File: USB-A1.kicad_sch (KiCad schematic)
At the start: 24 parts, among them J10 USB3_A, J9 USB3_A, U16 UCS2114-1-V/G4, U17 TPD4E02B04DQA, U18 TPD4E02B04DQA

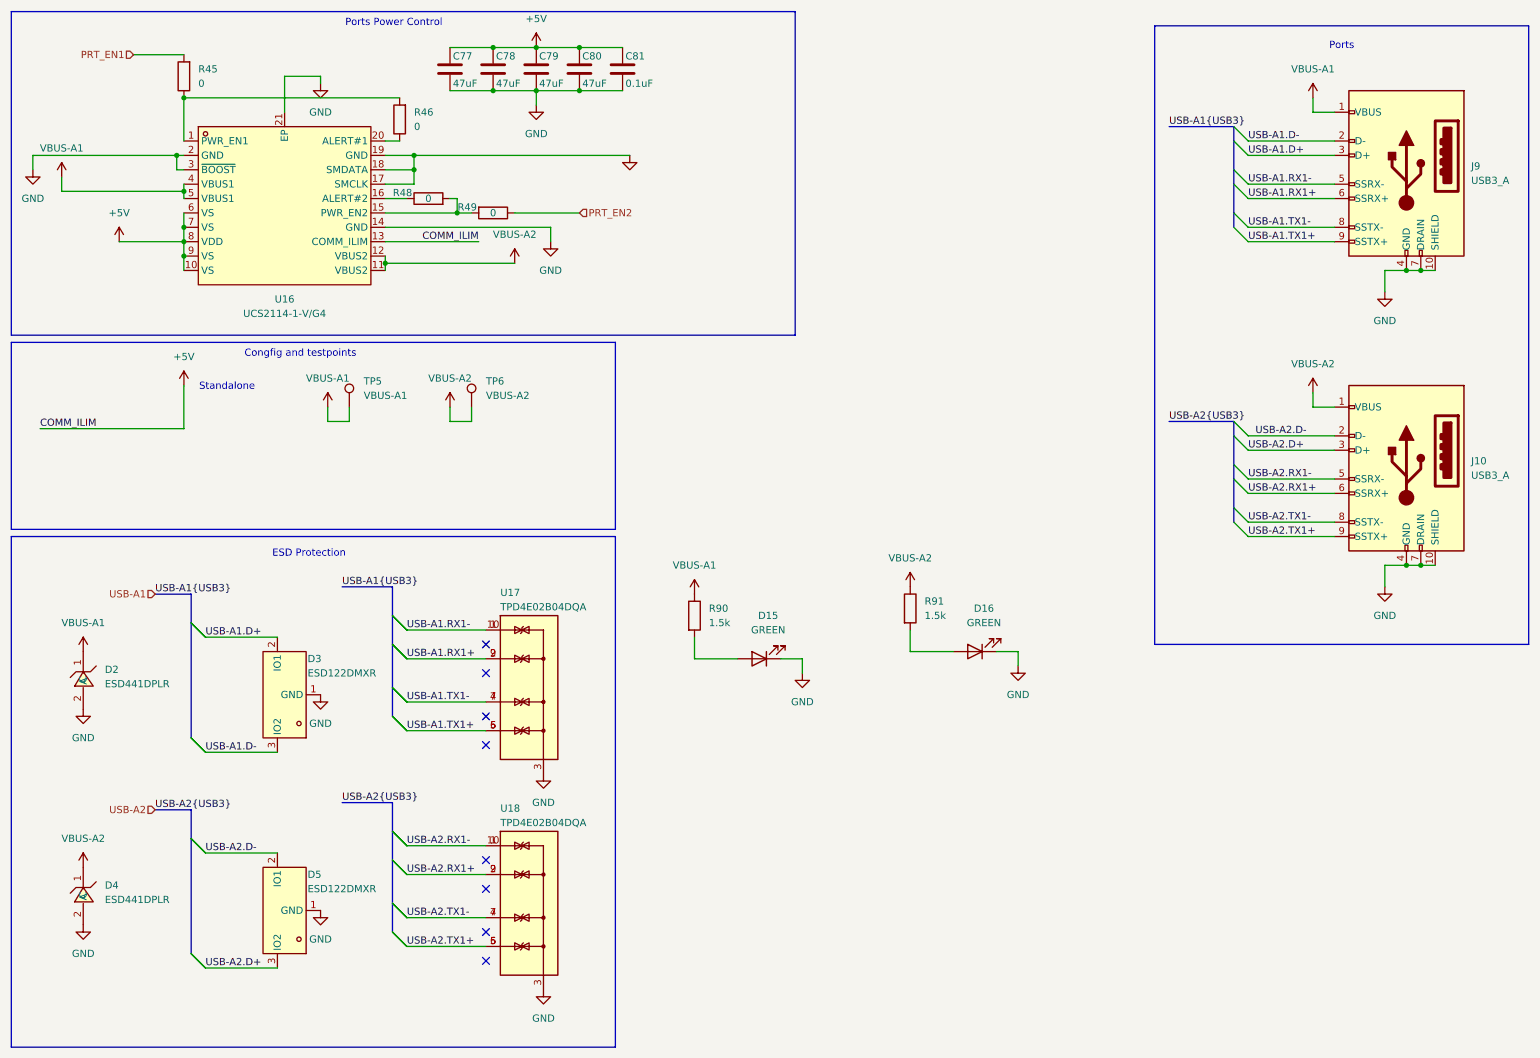
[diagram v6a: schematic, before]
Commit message: Ferrite Breads added for 5V, TVS and ESD diodes added
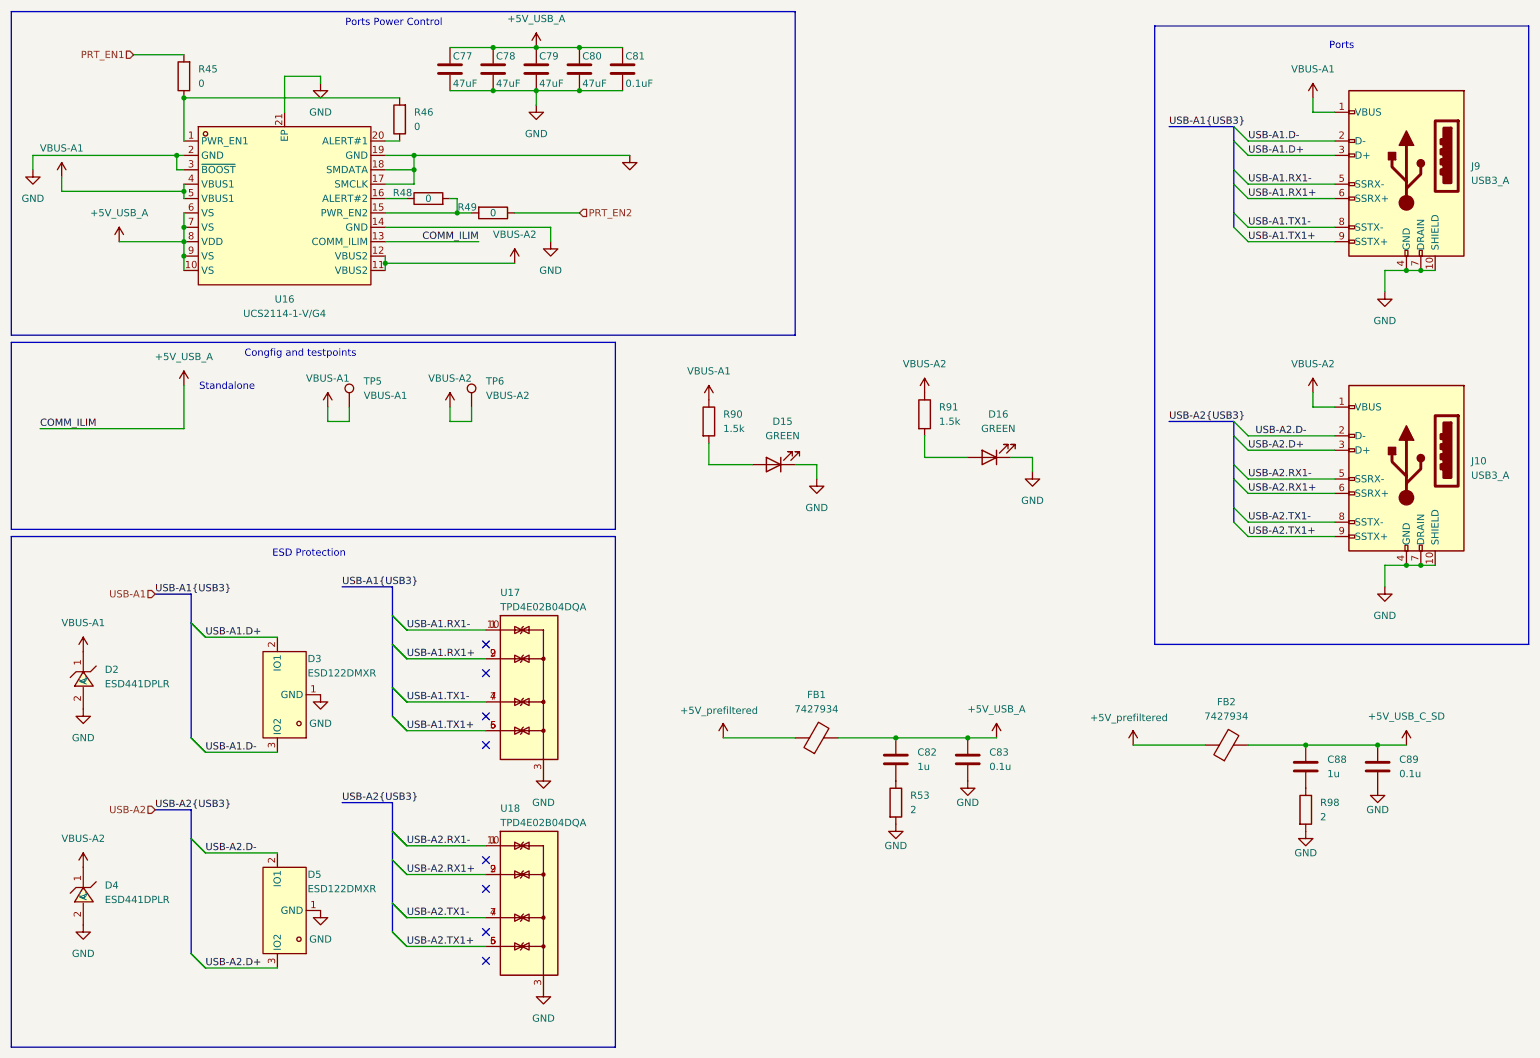
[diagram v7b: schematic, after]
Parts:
- added C82, C88: 1u, symbol Device:C
- added C83, C89: 0.1u, symbol Device:C
- added FB1, FB2: 7427934, symbol Device:FerriteBead
- added R53, R98: 2, symbol Device:R
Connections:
- net GND: now also C83.2, C89.2, R53.2, R98.2
- net +5V renamed +5V_USB_A
- net +5V_USB_A: now also C82.1, C83.1, FB1.2
- new net: C82.2, R53.1
- new net: C88.2, R98.1
- new net +5V_USB_C_SD: C88.1, C89.1, FB2.2
- new net +5V_prefiltered: FB1.1, FB2.1
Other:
- moved on the sheet: D15, D16, R90, R91

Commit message: Ferrite bread filter for LDO and MIC23201, labelling improved
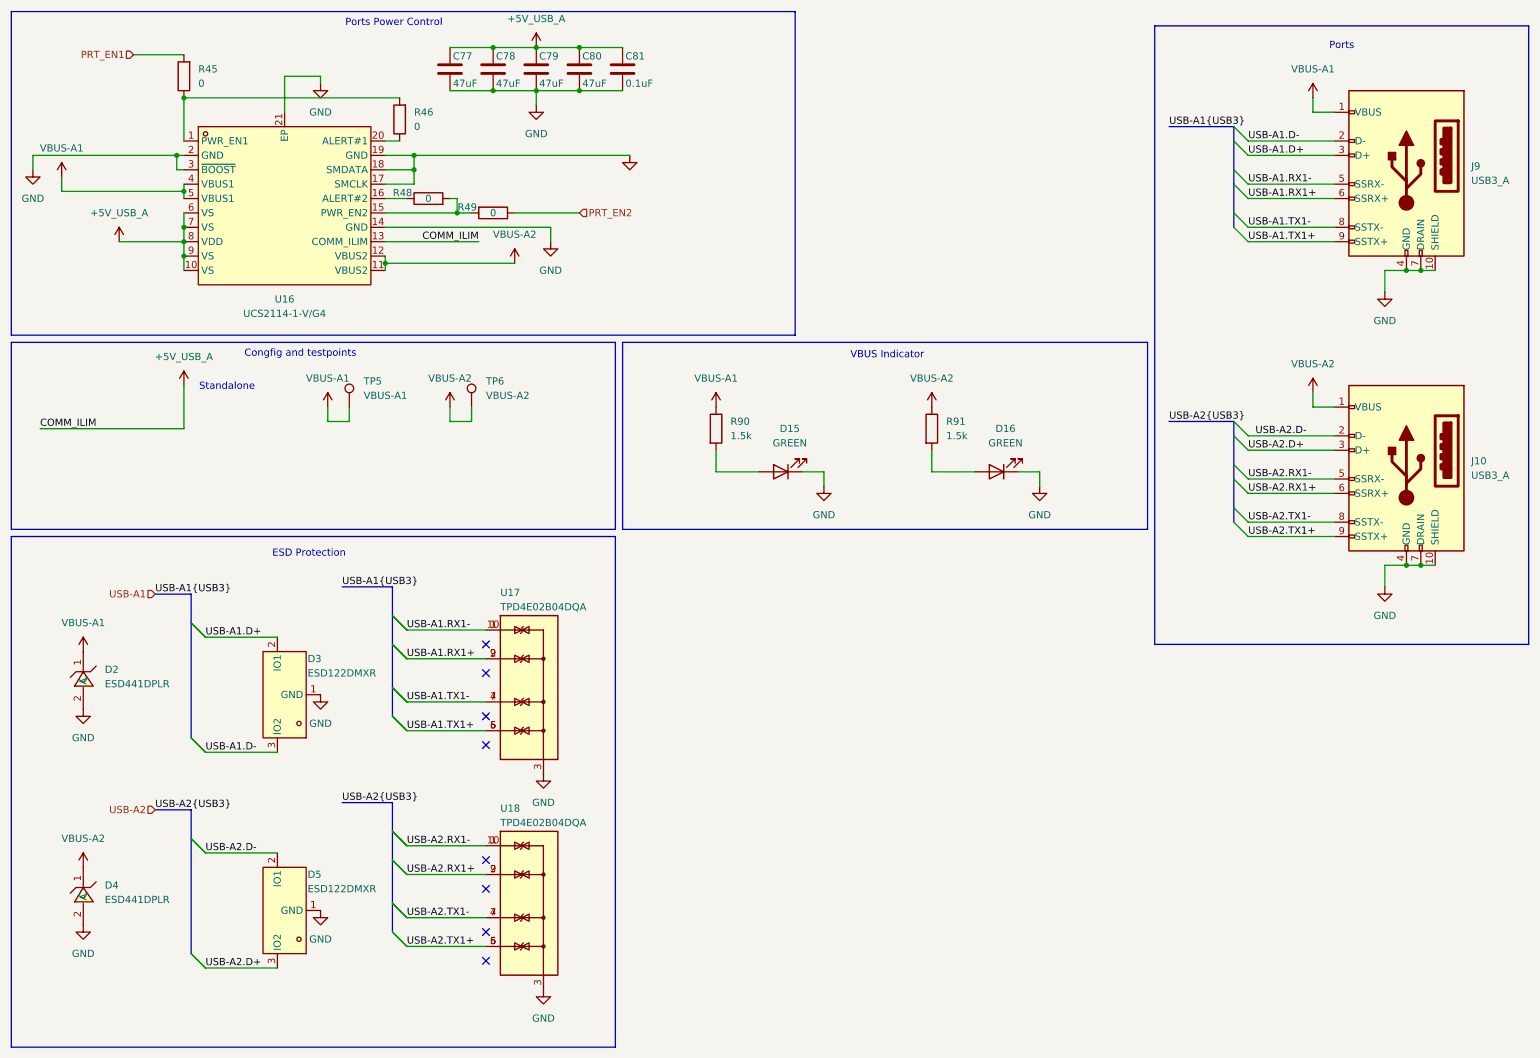
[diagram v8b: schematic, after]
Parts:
- removed C82, C88: 1u, symbol Device:C
- removed C83, C89: 0.1u, symbol Device:C
- removed FB1, FB2: 7427934, symbol Device:FerriteBead
- removed R53, R98: 2, symbol Device:R
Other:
- note added: "VBUS Indicator"
- moved on the sheet: D15, D16, R90, R91
